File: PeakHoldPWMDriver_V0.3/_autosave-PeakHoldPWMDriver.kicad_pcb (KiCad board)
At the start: 2 copper layers, 100.1 x 50 mm, 117 parts, among them J1 RND 205-00203, J2 RND 205-00205, Q1 2N7002, Q10 2N7002, Q11 2N7002, Q12 2N7002, Q13 TSM2309, Q14 IRLL 024N, Q15 TSM2309, Q16 IRLL 024N, Q17 TSM2309, Q18 TSM2309, Q19 TSM2309, Q2 2N7002, Q20 TSM2309, Q3 2N7002, Q4 2N7002, Q5 TSM2309, Q6 TSM2309, Q7 IRLL 024N, Q8 IRLL 024N, Q9 2N7002, U1 74LS32, U2 LM2901, U3 74LS74, U4 LTC6992, U5 74LS74, U6 LM340, U7 74LS08, U8 74LS08

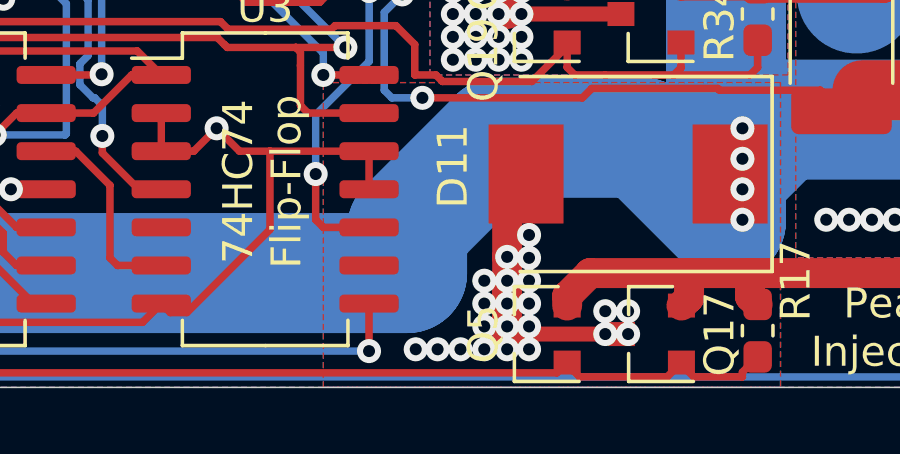
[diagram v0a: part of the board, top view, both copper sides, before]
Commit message: Updates on schematic and pcb because of heat
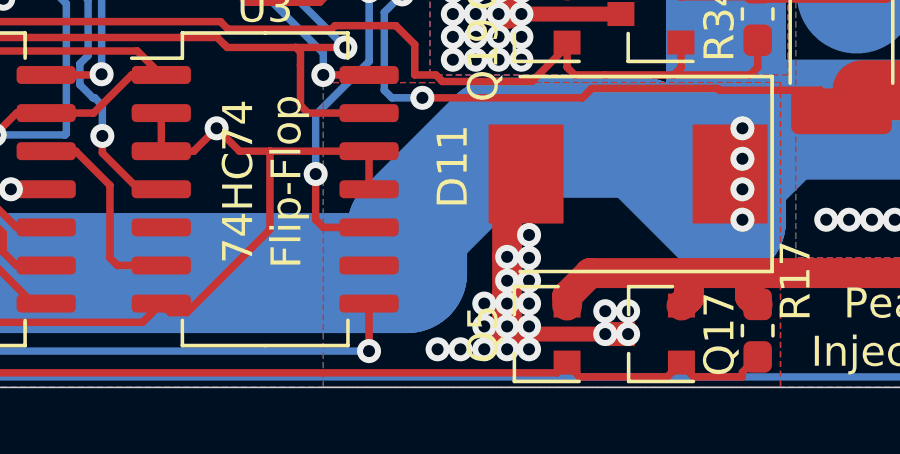
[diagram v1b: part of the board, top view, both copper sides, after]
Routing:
- net Net-(D11-Pad2): vias 22 -> 20
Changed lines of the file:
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@@
     (thickness 1.6)
     (drawings 18)
-    (tracks 1939)
+    (tracks 1937)
     (zones 0)
     (modules 117)
@@
     (effects (font (size 1.5 1.5) (thickness 0.3)))
   )
-  (via (at 179.102 112.522) (size 0.8) (drill 0.4) (layers F.Cu B.Cu) (net 68))
   (via (at 179.102 113.284) (size 0.8) (drill 0.4) (layers F.Cu B.Cu) (net 68))
   (via (at 179.102 114.046) (size 0.8) (drill 0.4) (layers F.Cu B.Cu) (net 68))
   (via (at 179.102 114.808) (size 0.8) (drill 0.4) (layers F.Cu B.Cu) (net 68))
-  (via (at 176.816 114.808) (size 0.8) (drill 0.4) (layers F.Cu B.Cu) (net 68))
   (via (at 177.038 68.834) (size 0.8) (drill 0.4) (layers F.Cu B.Cu) (net 1))
   (segment (start 175.327 68.834) (end 173.736 68.834) (width 0.25) (layer F.Cu) (net 1) (status 10))
@@
     (connect_pads (clearance 0.254))
     (min_thickness 0.254)
-    (fill (arc_segments 32) (thermal_gap 0.508) (thermal_bridge_width 0.508))
+    (fill yes (arc_segments 32) (thermal_gap 0.508) (thermal_bridge_width 0.508))
     (polygon
       (pts
@@
     (connect_pads (clearance 0.254))
     (min_thickness 0.254)
-    (fill (arc_segments 32) (thermal_gap 0.508) (thermal_bridge_width 0.508))
+    (fill yes (arc_segments 32) (thermal_gap 0.508) (thermal_bridge_width 0.508))
     (polygon
       (pts
@@
     (connect_pads yes (clearance 0.254))
     (min_thickness 0.254)
-    (fill (arc_segments 32) (thermal_gap 0.508) (thermal_bridge_width 0.508))
+    (fill yes (arc_segments 32) (thermal_gap 0.508) (thermal_bridge_width 0.508))
     (polygon
       (pts
@@
     (connect_pads yes (clearance 0.254))
     (min_thickness 0.254)
-    (fill (arc_segments 32) (thermal_gap 0.508) (thermal_bridge_width 0.508))
+    (fill yes (arc_segments 32) (thermal_gap 0.508) (thermal_bridge_width 0.508))
     (polygon
       (pts
@@
     (connect_pads yes (clearance 0.254))
     (min_thickness 0.254)
-    (fill (arc_segments 32) (thermal_gap 0.508) (thermal_bridge_width 0.508))
+    (fill yes (arc_segments 32) (thermal_gap 0.508) (thermal_bridge_width 0.508))
     (polygon
       (pts
@@
     (connect_pads yes (clearance 0.254))
     (min_thickness 0.254)
-    (fill (arc_segments 32) (thermal_gap 0.508) (thermal_bridge_width 0.508))
+    (fill yes (arc_segments 32) (thermal_gap 0.508) (thermal_bridge_width 0.508))
     (polygon
       (pts
@@
     (connect_pads yes (clearance 0.254))
     (min_thickness 0.254)
-    (fill (arc_segments 32) (thermal_gap 0.508) (thermal_bridge_width 0.508))
+    (fill yes (arc_segments 32) (thermal_gap 0.508) (thermal_bridge_width 0.508))
     (polygon
       (pts
@@
     (connect_pads yes (clearance 0.254))
     (min_thickness 0.254)
-    (fill (arc_segments 32) (thermal_gap 0.508) (thermal_bridge_width 0.508))
+    (fill yes (arc_segments 32) (thermal_gap 0.508) (thermal_bridge_width 0.508))
     (polygon
       (pts
@@
     (connect_pads yes (clearance 0.254))
     (min_thickness 0.254)
-    (fill (arc_segments 32) (thermal_gap 0.508) (thermal_bridge_width 0.508))
+    (fill yes (arc_segments 32) (thermal_gap 0.508) (thermal_bridge_width 0.508))
     (polygon
       (pts
@@
     (connect_pads yes (clearance 0.254))
     (min_thickness 0.254)
-    (fill (arc_segments 32) (thermal_gap 0.508) (thermal_bridge_width 0.508))
+    (fill yes (arc_segments 32) (thermal_gap 0.508) (thermal_bridge_width 0.508))
     (polygon
       (pts
@@
     (connect_pads yes (clearance 0.254))
     (min_thickness 0.254)
-    (fill (arc_segments 32) (thermal_gap 0.254) (thermal_bridge_width 0.255) (smoothing fillet))
+    (fill yes (arc_segments 32) (thermal_gap 0.254) (thermal_bridge_width 0.255) (smoothing fillet))
     (polygon
       (pts
@@
     (connect_pads yes (clearance 0.254))
     (min_thickness 0.254)
-    (fill (arc_segments 32) (thermal_gap 0.508) (thermal_bridge_width 0.508) (smoothing fillet))
+    (fill yes (arc_segments 32) (thermal_gap 0.508) (thermal_bridge_width 0.508) (smoothing fillet))
     (polygon
       (pts
@@
     (connect_pads yes (clearance 0.254))
     (min_thickness 0.254)
-    (fill (arc_segments 32) (thermal_gap 0.508) (thermal_bridge_width 0.508) (smoothing fillet))
+    (fill yes (arc_segments 32) (thermal_gap 0.508) (thermal_bridge_width 0.508) (smoothing fillet))
     (polygon
       (pts
@@
     (connect_pads yes (clearance 0.254))
     (min_thickness 0.254)
-    (fill (arc_segments 32) (thermal_gap 0.508) (thermal_bridge_width 0.508) (smoothing fillet))
+    (fill yes (arc_segments 32) (thermal_gap 0.508) (thermal_bridge_width 0.508) (smoothing fillet))
     (polygon
       (pts
@@
     (connect_pads yes (clearance 0.254))
     (min_thickness 0.254)
-    (fill (arc_segments 32) (thermal_gap 0.508) (thermal_bridge_width 0.508) (smoothing fillet))
+    (fill yes (arc_segments 32) (thermal_gap 0.508) (thermal_bridge_width 0.508) (smoothing fillet))
     (polygon
       (pts
@@
     (connect_pads yes (clearance 0.254))
     (min_thickness 0.254)
-    (fill (arc_segments 32) (thermal_gap 0.508) (thermal_bridge_width 0.508) (smoothing fillet))
+    (fill yes (arc_segments 32) (thermal_gap 0.508) (thermal_bridge_width 0.508) (smoothing fillet))
     (polygon
       (pts
@@
     (connect_pads yes (clearance 0.254))
     (min_thickness 0.254)
-    (fill (arc_segments 32) (thermal_gap 0.508) (thermal_bridge_width 0.508) (smoothing fillet))
+    (fill yes (arc_segments 32) (thermal_gap 0.508) (thermal_bridge_width 0.508) (smoothing fillet))
     (polygon
       (pts
@@
     (connect_pads yes (clearance 0.254))
     (min_thickness 0.254)
-    (fill (arc_segments 32) (thermal_gap 0.508) (thermal_bridge_width 0.508) (smoothing fillet))
+    (fill yes (arc_segments 32) (thermal_gap 0.508) (thermal_bridge_width 0.508) (smoothing fillet))
     (polygon
       (pts
@@
     (connect_pads yes (clearance 0.254))
     (min_thickness 0.254)
-    (fill (arc_segments 32) (thermal_gap 0.508) (thermal_bridge_width 0.508) (smoothing fillet))
+    (fill yes (arc_segments 32) (thermal_gap 0.508) (thermal_bridge_width 0.508) (smoothing fillet))
     (polygon
       (pts
